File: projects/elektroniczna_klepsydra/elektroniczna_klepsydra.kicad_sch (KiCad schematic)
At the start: 29 parts, among them J1 +, J2 -, SW1 SW_Push, T1 BC548, T2 BC548, T3 BC548, T4 BC558, T5 BC548, T6 BC558, T7 BC558, Y1 3V

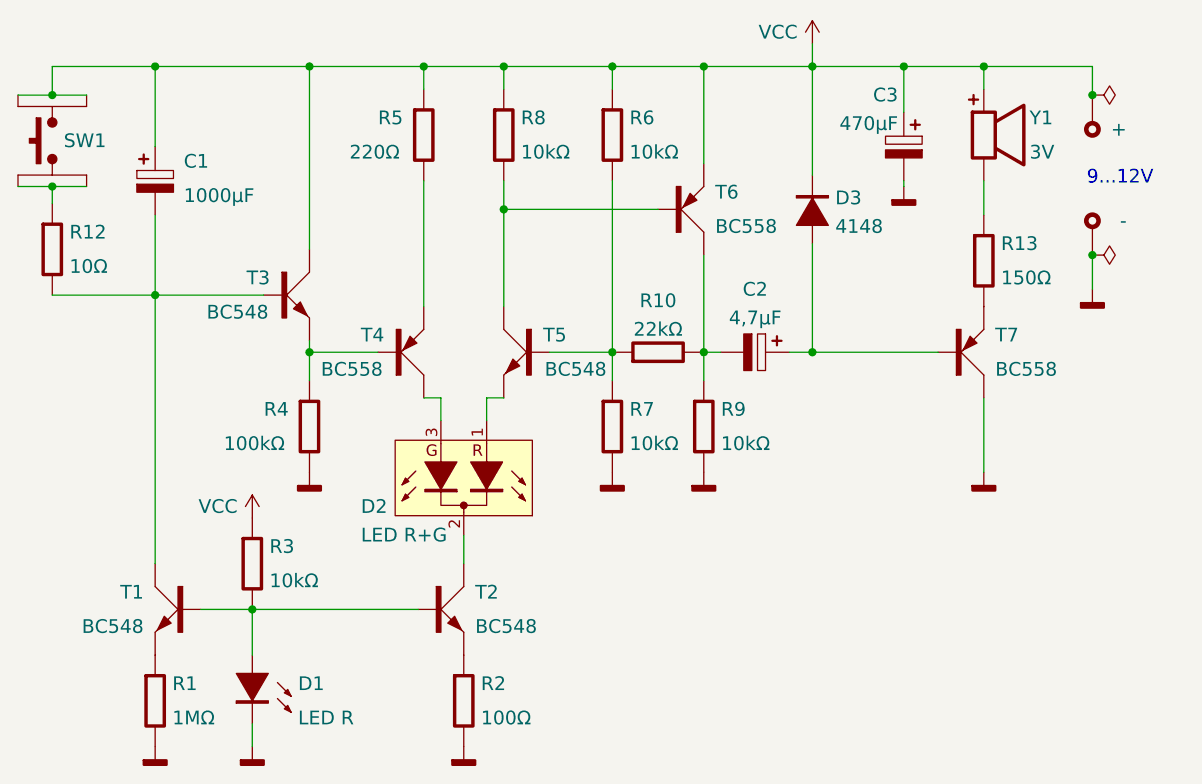
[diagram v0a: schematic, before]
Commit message: Added a few new symbols to library; new OŁ project (tester_refleksu)
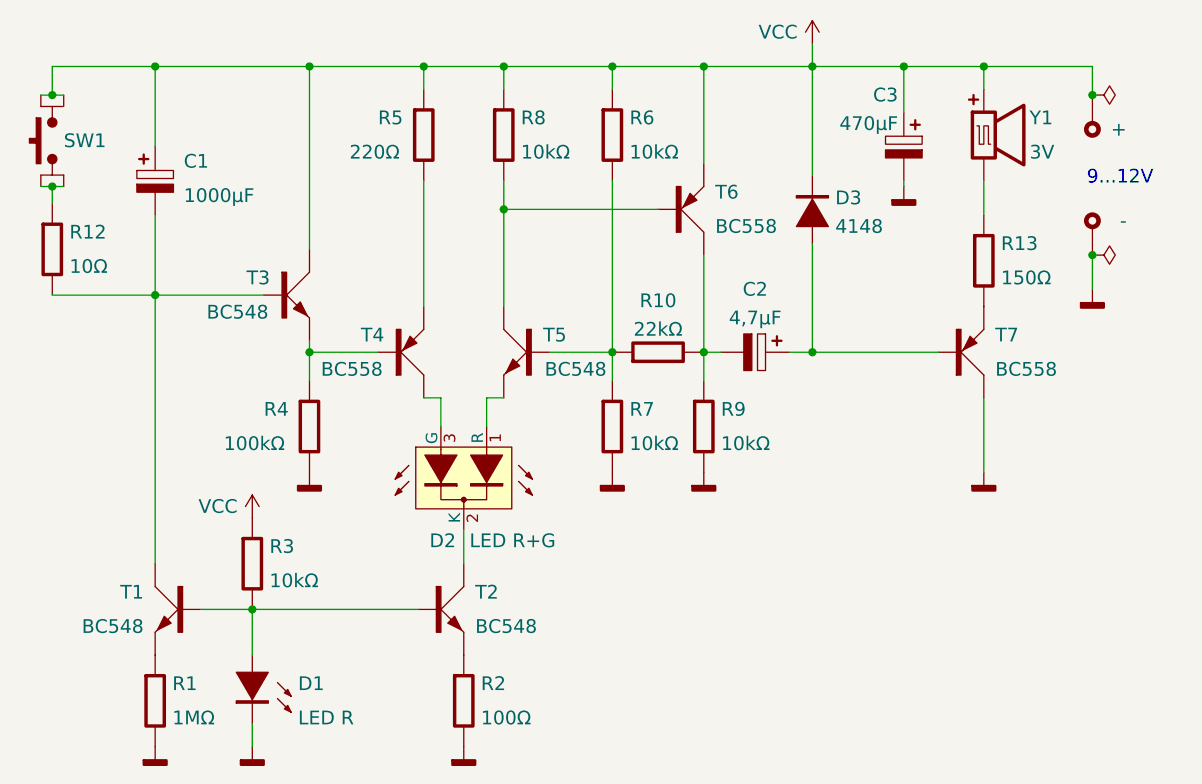
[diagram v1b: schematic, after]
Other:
- moved on the sheet: SW1
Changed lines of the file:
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@@
   (junction (at 97.155 62.865) (diameter 0) (color 0 0 0 0)
   )
+  (junction (at 191.77 59.69) (diameter 0) (color 0 0 0 0)
+  )
+  (junction (at 159.385 59.69) (diameter 0) (color 0 0 0 0)
+  )
+  (junction (at 212.725 80.645) (diameter 0) (color 0 0 0 0)
+  )
+  (junction (at 212.725 62.865) (diameter 0) (color 0 0 0 0)
+  )
+  (junction (at 159.385 91.44) (diameter 0) (color 0 0 0 0)
+  )
+  (junction (at 125.73 91.44) (diameter 0) (color 0 0 0 0)
+  )
+  (junction (at 147.32 75.565) (diameter 0) (color 0 0 0 0)
+  )
+  (junction (at 108.585 85.09) (diameter 0) (color 0 0 0 0)
+  )
+  (junction (at 169.545 91.44) (diameter 0) (color 0 0 0 0)
+  )
+  (junction (at 200.66 59.69) (diameter 0) (color 0 0 0 0)
+  )
   (junction (at 97.155 73.025) (diameter 0) (color 0 0 0 0)
   )
-  (junction (at 191.77 59.69) (diameter 0) (color 0 0 0 0)
-  )
-  (junction (at 159.385 59.69) (diameter 0) (color 0 0 0 0)
-  )
-  (junction (at 212.725 80.645) (diameter 0) (color 0 0 0 0)
-  )
-  (junction (at 212.725 62.865) (diameter 0) (color 0 0 0 0)
-  )
-  (junction (at 159.385 91.44) (diameter 0) (color 0 0 0 0)
-  )
-  (junction (at 125.73 91.44) (diameter 0) (color 0 0 0 0)
-  )
-  (junction (at 147.32 75.565) (diameter 0) (color 0 0 0 0)
-  )
-  (junction (at 108.585 85.09) (diameter 0) (color 0 0 0 0)
-  )
-  (junction (at 169.545 91.44) (diameter 0) (color 0 0 0 0)
-  )
-  (junction (at 200.66 59.69) (diameter 0) (color 0 0 0 0)
-  )
   (junction (at 181.61 91.44) (diameter 0) (color 0 0 0 0)
   )
@@
   (junction (at 169.545 59.69) (diameter 0) (color 0 0 0 0)
   )
+  (wire (pts (xy 97.155 73.025) (xy 98.425 73.025))
+    (stroke (width 0) (type default) (color 0 0 0 0))
+  )
   (wire (pts (xy 159.385 59.69) (xy 169.545 59.69))
     (stroke (width 0) (type default) (color 0 0 0 0))
@@
     (stroke (width 0) (type default) (color 0 0 0 0))
   )
+  (wire (pts (xy 97.155 62.865) (xy 98.425 62.865))
+    (stroke (width 0) (type default) (color 0 0 0 0))
+  )
   (wire (pts (xy 212.725 80.645) (xy 212.725 84.455))
     (stroke (width 0) (type default) (color 0 0 0 0))
@@
     (stroke (width 0) (type default) (color 0 0 0 0))
   )
-  (wire (pts (xy 93.345 62.865) (xy 97.155 62.865))
-    (stroke (width 0) (type default) (color 0 0 0 0))
-  )
   (wire (pts (xy 138.43 59.69) (xy 125.73 59.69))
     (stroke (width 0) (type default) (color 0 0 0 0))
@@
     (stroke (width 0) (type default) (color 0 0 0 0))
   )
-  (wire (pts (xy 97.155 73.025) (xy 100.965 73.025))
+  (wire (pts (xy 95.885 73.025) (xy 97.155 73.025))
     (stroke (width 0) (type default) (color 0 0 0 0))
   )
@@
     (stroke (width 0) (type default) (color 0 0 0 0))
   )
-  (wire (pts (xy 145.415 96.52) (xy 145.415 99.06))
+  (wire (pts (xy 145.415 96.52) (xy 145.415 99.695))
     (stroke (width 0) (type default) (color 0 0 0 0))
   )
@@
     (stroke (width 0) (type default) (color 0 0 0 0))
   )
-  (wire (pts (xy 140.335 96.52) (xy 140.335 99.06))
+  (wire (pts (xy 140.335 96.52) (xy 140.335 99.695))
     (stroke (width 0) (type default) (color 0 0 0 0))
   )
@@
     (stroke (width 0) (type default) (color 0 0 0 0))
   )
-  (wire (pts (xy 97.155 62.865) (xy 100.965 62.865))
-    (stroke (width 0) (type default) (color 0 0 0 0))
-  )
-  (wire (pts (xy 93.345 73.025) (xy 97.155 73.025))
+  (wire (pts (xy 95.885 62.865) (xy 97.155 62.865))
     (stroke (width 0) (type default) (color 0 0 0 0))
   )
@@
     (stroke (width 0) (type default) (color 0 0 0 0))
   )
-  (wire (pts (xy 142.875 111.76) (xy 142.875 114.935))
+  (wire (pts (xy 142.875 111.125) (xy 142.875 114.935))
     (stroke (width 0) (type default) (color 0 0 0 0))
   )
@@
     (pin "2")
   )
-  (symbol (lib_id "Custom_Generic:LED_RKG") (at 142.875 104.14 90) (mirror x) (unit 1)
-    (in_bom yes) (on_board yes)
-    (property "Reference" "D2" (id 0) (at 131.445 108.585 90)
+  (symbol (lib_id "Custom_Generic:LED_RKG") (at 142.875 104.775 90) (mirror x) (unit 1)
+    (in_bom yes) (on_board yes)
+    (property "Reference" "D2" (id 0) (at 139.065 112.395 90)
       (effects (font (size 1.524 1.524)) (justify right))
     )
-    (property "Value" "LED R+G" (id 1) (at 131.445 111.76 90)
+    (property "Value" "LED R+G" (id 1) (at 143.51 112.395 90)
       (effects (font (size 1.524 1.524)) (justify right))
     )
-    (property "Footprint" "VeeCad:LED_5_3P" (id 2) (at 147.32 116.713 0)
-      (effects (font (size 1.27 1.27)) hide)
-    )
-    (property "Datasheet" "" (id 3) (at 145.415 105.41 0)
-      (effects (font (size 1.27 1.27)) hide)
-    )
+    (property "Footprint" "VeeCad:LED_5_3P" (id 2) (at 147.32 117.348 0)
+      (effects (font (size 1.27 1.27)) hide)
+    )
+    (property "Datasheet" "" (id 3) (at 145.415 106.045 0)
+      (effects (font (size 1.27 1.27)) hide)
+    )
